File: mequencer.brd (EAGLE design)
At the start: 102.5 x 80 mm, 71 parts, among them IC1 NE555D, IC10 LF353D, IC11 NE555D, IC12 NE555D, IC2 4163D, IC3 74HC85D, IC4 4051D, IC5 4051D, IC6 74HCT04D, IC7 4051D, IC8 4051D, IC9 LF353D, U1 74LVC1G08SE-7

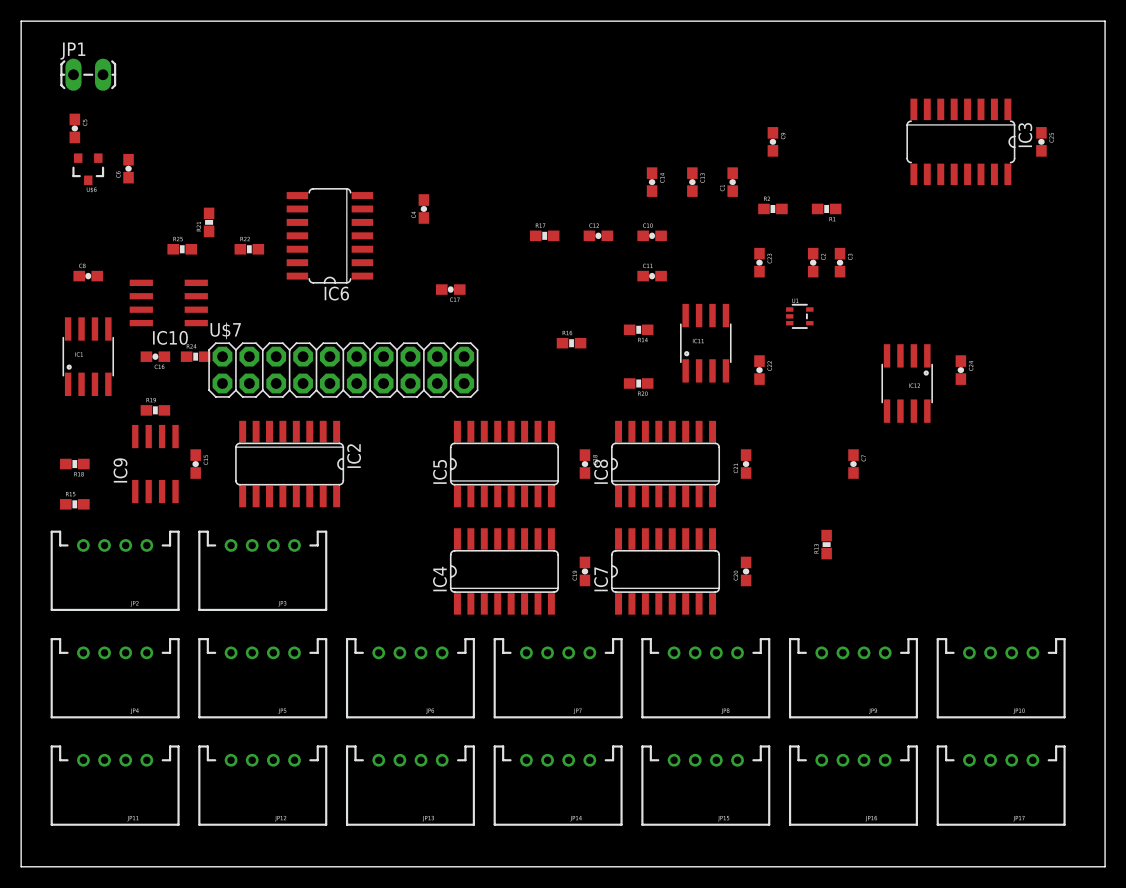
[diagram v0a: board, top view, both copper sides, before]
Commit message: through hole led on mini boards
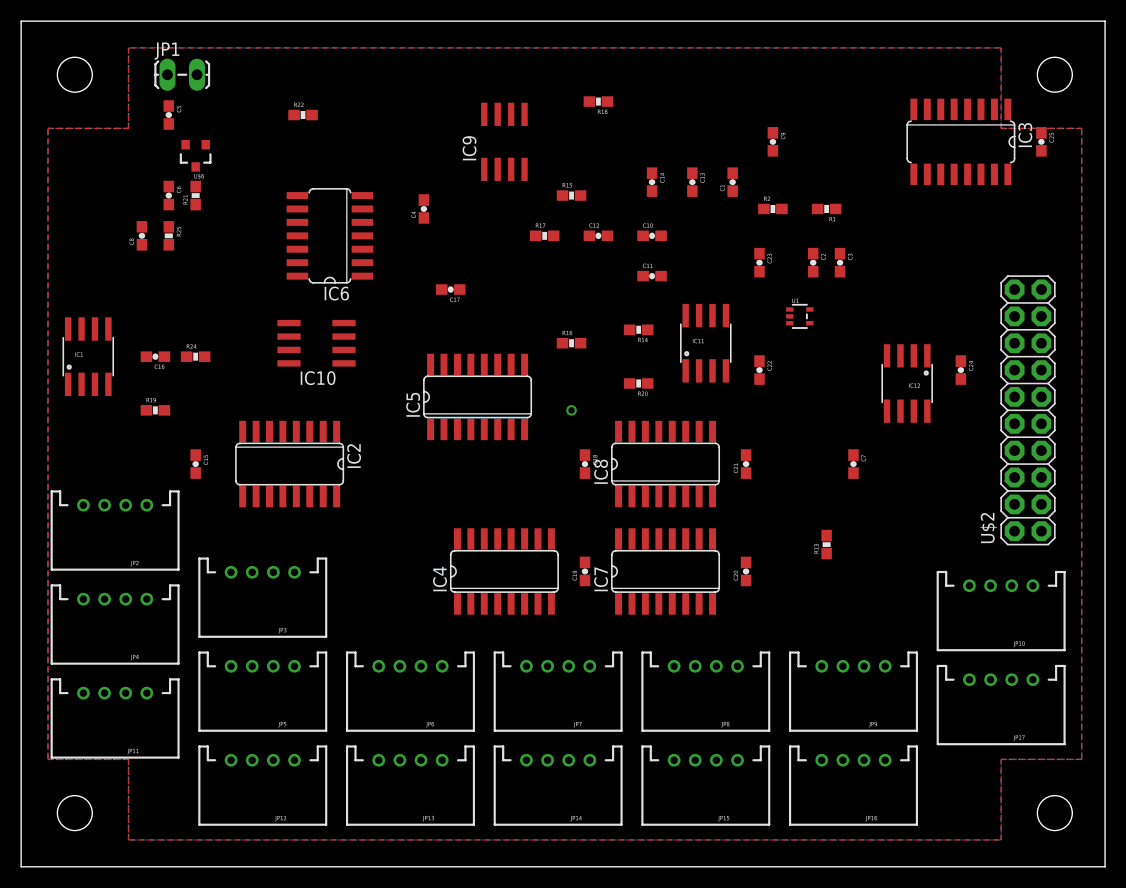
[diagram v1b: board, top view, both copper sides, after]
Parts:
- removed U$7: M10X2, SparkFun-Connectors:2X10
- added STANDOFF1, STANDOFF2, STANDOFF3, STANDOFF4: STAND-OFF, SparkFun-Electromechanical:STAND-OFF
- added U$2: M10X2, SparkFun-Connectors:2X10
- moved R18 60.2 mm to (50.8, 72.4)
- moved R15 55.3 mm to (48.3, 63.5)
- moved IC9 44.9 mm to (41.9, 68.6)
- moved IC10 14.5 mm to (24.1, 49.5)
- moved R22 13.7 mm to (22.9, 71.1)
- moved U$6 10.2 mm to (12.7, 67.3)
- moved C5 8.98 mm to (10.2, 71.1)
- moved JP1 8.89 mm to (10.2, 74.9)
- moved JP17 7.62 mm to (88.9, 12.7)
- moved IC5 6.84 mm to (39.4, 44.5)
- moved JP10 6.35 mm to (88.9, 21.6)
- moved JP11 6.35 mm to (5.08, 11.4)
- moved C8 6.35 mm to (7.62, 59.7), turned to 90 degrees
- moved JP4 5.08 mm to (5.08, 20.3)
- moved C6 4.58 mm to (10.2, 63.5), turned to 270 degrees
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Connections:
- removed net N$6: U$7.18
- net 5V: now also U$2.1; no longer U$7.1
- net CLOCK: now also U$2.5; no longer U$7.5
- net CLOCK_SPEED: now also U$2.7; no longer U$7.7
- net CV: now also U$2.17; no longer U$7.14
- net GND: now also U$2.20; no longer U$7.20
- net INT_CLOCK: now also U$2.3; no longer U$7.3
- net LOAD: now also U$2.11; no longer U$7.11
- net LOAD0: now also U$2.8; no longer U$7.6
- net LOAD1: now also U$2.6; no longer U$7.8
- net LOAD2: now also U$2.4; no longer U$7.10
- net LOAD3: now also U$2.2; no longer U$7.12
- net NOTE_LENGTH: now also U$2.9; no longer U$7.9
- net RESET0: now also U$2.16; no longer U$7.13
- net RESET1: now also U$2.14; no longer U$7.15
- net RESET2: now also U$2.12; no longer U$7.2
- net RESET3: now also U$2.10; no longer U$7.4
- net TRIG: now also U$2.19; no longer U$7.16
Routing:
- added copper zone on layer 16, net N$1
- added copper zone on layer 1, net N$5

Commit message: Moving shit around
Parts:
- moved C25 86.0 mm to (7.62, 55.9)
- moved R19 84.4 mm to (92.7, 53.3)
- moved R25 65.0 mm to (74.9, 54.6), turned to 0 degrees
- moved R22 64.8 mm to (81.3, 43.2), turned to 90 degrees
- moved R21 55.0 mm to (67.3, 57.1), turned to 270 degrees
- moved C2 53.9 mm to (19.1, 71.1), turned to 90 degrees
- moved R1 53.6 mm to (20.3, 74.9)
- moved R2 52.4 mm to (16.5, 74.9), turned to 90 degrees
- moved C1 51.2 mm to (12.7, 71.1), turned to 180 degrees
- moved IC10 50.3 mm to (73.7, 58.4)
- moved C11 50.2 mm to (7.62, 41.9), turned to 90 degrees
- moved C15 49.1 mm to (61.0, 29.2)
- moved IC9 48.1 mm to (88.9, 58.4), turned to 270 degrees
- moved C18 46.2 mm to (88.9, 62.2), turned to 0 degrees
- moved C4 44.6 mm to (78.7, 66.0), turned to 0 degrees
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
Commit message: Moving shit around more
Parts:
- removed C20, C21, C22, C23, C24, C25: .1uF, SparkFun-Capacitors:0603-CAP
- moved C15 59.6 mm to (7.62, 55.9)
- moved C16 41.3 mm to (73.7, 54.6), turned to 180 degrees
- moved C17 14.5 mm to (73.7, 40.6), turned to 180 degrees
- moved C18 14.0 mm to (88.9, 48.3)
- moved C4 10.5 mm to (81.3, 55.9)
- moved R25 8.98 mm to (73.7, 63.5)
- moved R19 8.98 mm to (91.4, 62.2), turned to 180 degrees
- moved R18 8.89 mm to (87.6, 62.2)
- moved C3 7.62 mm to (73.7, 48.3)
- moved R13 4.58 mm to (83.8, 40.6)
- moved R21 3.59 mm to (64.8, 59.7)
- moved R24 3.59 mm to (52.1, 41.9), turned to 180 degrees
- moved R22 2.54 mm to (81.3, 45.7), turned to 270 degrees
- moved R20 2.54 mm to (69.8, 63.5)
- moved C9 1.27 mm to (61.0, 69.8)
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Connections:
- net 5V: no longer C20.2, C21.2, C22.2, C23.2, C24.2, C25.2
- net N$7: no longer C20.1, C21.1, C22.1, C23.1, C24.1, C25.1

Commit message: stuff
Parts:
- moved IC5 43.5 mm to (50.2, 31.8), turned to 180 degrees
- moved C14 43.5 mm to (62.6, 41.5)
- moved R24 33.1 mm to (80.0, 59.7), turned to 0 degrees
- moved R14 30.0 mm to (66.7, 43.8), turned to 270 degrees
- moved C19 27.7 mm to (74.3, 24.8), turned to 180 degrees
- moved IC6 25.6 mm to (72.4, 32.4)
- moved IC8 25.3 mm to (35.6, 31.8), turned to 180 degrees
- moved C10 25.2 mm to (40.6, 25.4), turned to 180 degrees
- moved C9 24.8 mm to (36.2, 69.2), turned to 90 degrees
- moved IC7 22.4 mm to (50.2, 44.5), turned to 180 degrees
- moved IC4 21.7 mm to (35.6, 44.5), turned to 180 degrees
- moved U$2 16.0 mm to (58.4, 64.1), turned to 90 degrees
- moved C13 12.9 mm to (50.2, 59.1), turned to 90 degrees
- moved IC2 12.5 mm to (43.2, 59.1)
- moved IC3 10.2 mm to (43.2, 69.2), turned to 0 degrees
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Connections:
- removed net N$7: C10.1, C11.1, C12.1, C13.1, C14.1, C15.1, C16.1, C17.1, C18.1, C19.1, C7.1, C8.1, C9.1, IC10.8, IC2.16, IC3.16, IC4.16, IC5.16, IC6.14, IC7.16, IC8.16, IC9.8
- net 5V: now also IC10.8, IC2.16, IC3.16, IC4.16, IC5.16, IC6.14, IC7.16, IC8.16, IC9.8
- net GND: now also C10.1, C11.1, C12.1, C13.1, C14.1, C15.1, C16.1, C17.1, C18.1, C19.1, C7.1, C8.1, C9.1
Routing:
- net VCC: track 0.00 -> 110.3 mm
- net 5V: track 0.00 -> 102.1 mm
- net COUNT2: track 0.00 -> 60.1 mm
- net COUNT1: track 0.00 -> 59.6 mm, vias 0 -> 2
- net COUNT3: track 0.00 -> 25.0 mm, vias 0 -> 2
- net N$4: track 0.00 -> 15.5 mm
- net COUNT0: track 0.00 -> 13.2 mm
- net N$27: track 0.00 -> 6.96 mm
- net N$3: track 0.00 -> 5.42 mm
- net N$2: track 0.00 -> 2.35 mm
- added copper zone on layer 1, net GND
- added copper zone on layer 16, net GND
- removed copper zone on layer 16, net N$1
- removed copper zone on layer 1, net N$5

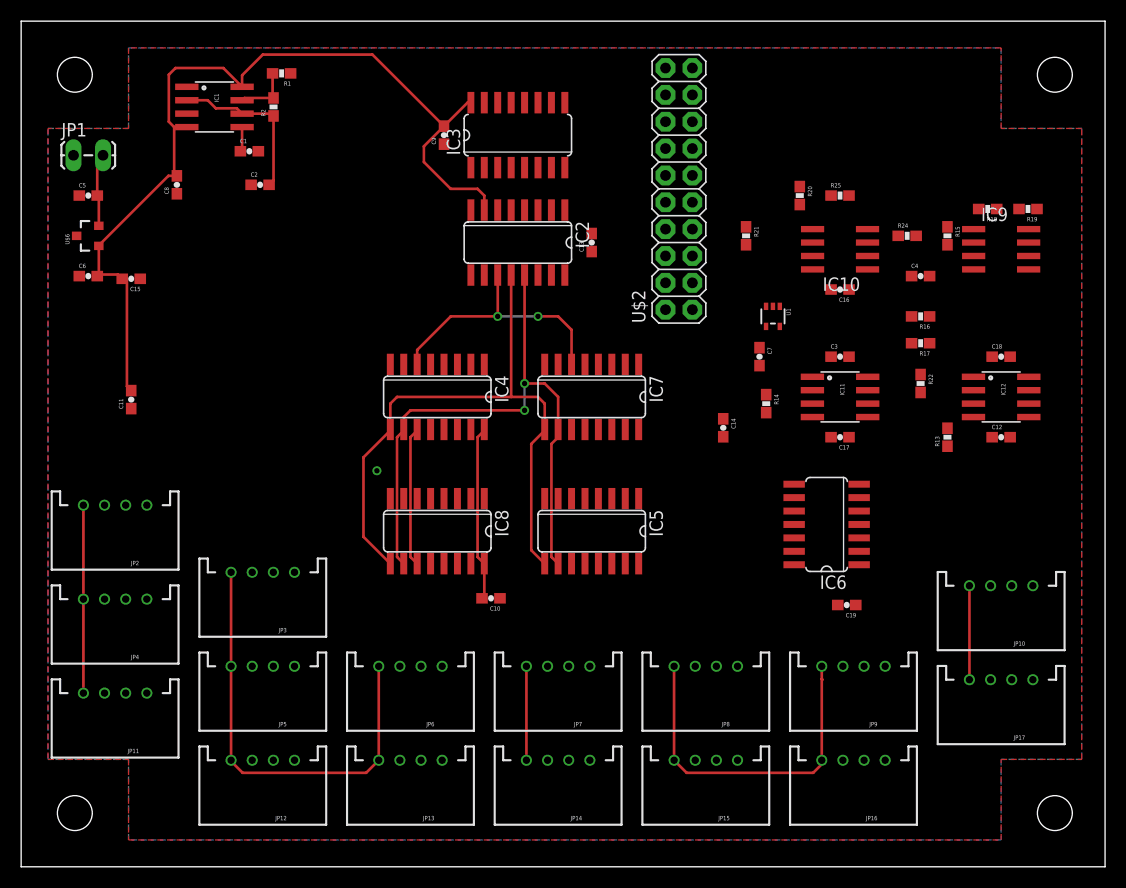
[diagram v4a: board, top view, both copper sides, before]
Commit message: Muxxes all wired up
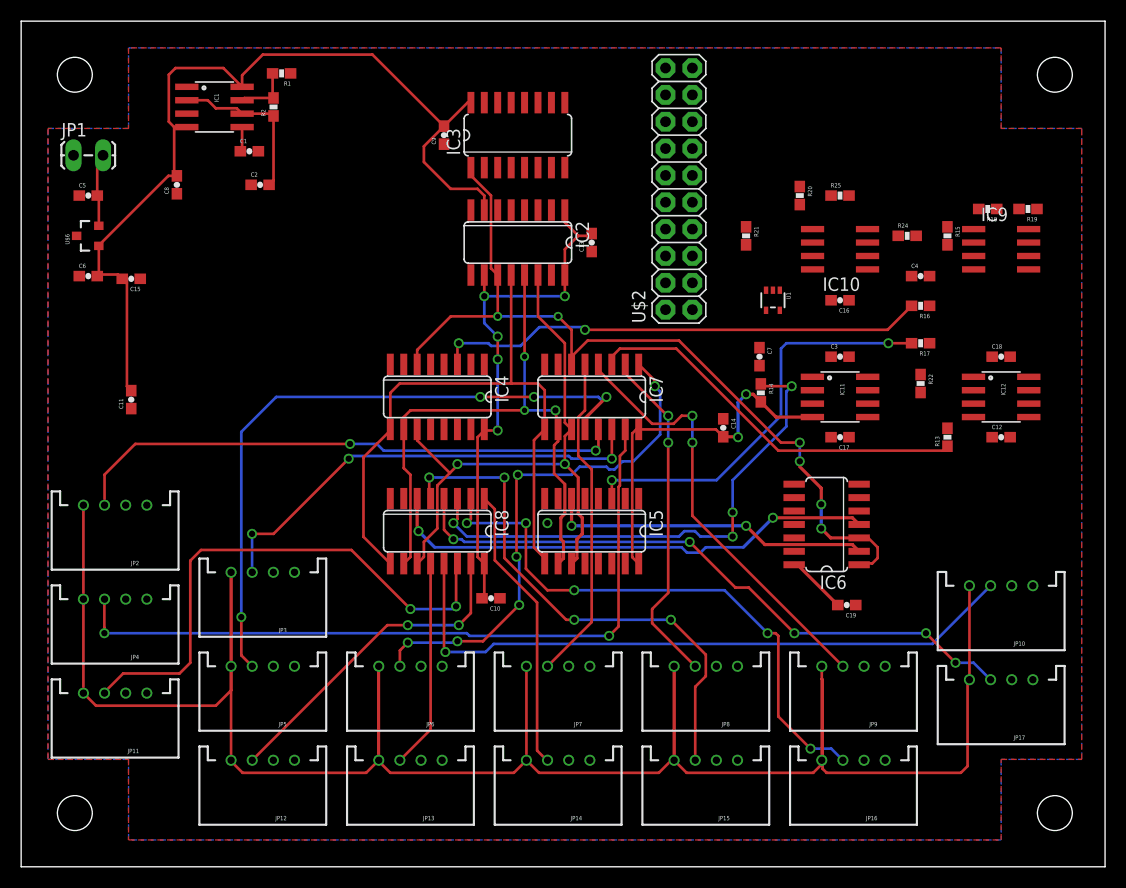
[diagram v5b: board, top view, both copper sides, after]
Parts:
- moved U1 1.52 mm to (67.3, 53.6)
- moved R14 1.14 mm to (66.2, 44.8)
- moved C16 1.02 mm to (73.7, 53.6)
- moved R16 1.00 mm to (81.3, 53.1)
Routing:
- net VCC: track 110.3 -> 215.0 mm
- net 5V: track 102.1 -> 177.1 mm, vias 0 -> 7
- net LED2: track 0.00 -> 71.2 mm, vias 0 -> 2
- net LED3: track 0.00 -> 62.7 mm, vias 0 -> 4
- net LED8: track 0.00 -> 62.6 mm, vias 0 -> 1
- net LED15: track 0.00 -> 60.5 mm, vias 0 -> 5
- net COUNT3: track 25.0 -> 81.2 mm, vias 2 -> 6
- net LED14: track 0.00 -> 54.3 mm, vias 0 -> 5
- net LED0: track 0.00 -> 52.9 mm, vias 0 -> 2
- net LED9: track 0.00 -> 51.1 mm, vias 0 -> 2
- net LED13: track 0.00 -> 50.0 mm, vias 0 -> 4
- net LED4: track 0.00 -> 49.8 mm, vias 0 -> 6
- net N$19: track 0.00 -> 49.4 mm, vias 0 -> 4
- net N$9: track 0.00 -> 47.3 mm, vias 0 -> 2
- net LOW_OUT: track 0.00 -> 46.8 mm, vias 0 -> 2
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
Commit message: main board all wired up
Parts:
- moved IC3 14.5 mm to (28.7, 69.2)
- moved C13 14.0 mm to (36.2, 57.9)
- moved IC2 14.0 mm to (29.2, 58.0)
- moved C9 14.0 mm to (22.2, 69.2)
- moved R21 3.94 mm to (68.7, 59.8)
- moved R24 1.17 mm to (79.8, 60.8), turned to 90 degrees
- moved R15 1.17 mm to (83.1, 60.6)
- moved C3 0.28 mm to (73.5, 48.5)
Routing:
- net 5V: track 177.1 -> 308.4 mm, vias 7 -> 17
- net CLOCK: track 0.00 -> 81.7 mm, vias 0 -> 4
- net CLOCK_SPEED: track 0.00 -> 62.7 mm
- net NOTE_LENGTH: track 0.00 -> 61.8 mm, vias 0 -> 2
- net INT_CLOCK: track 0.00 -> 60.0 mm
- net LOAD: track 0.00 -> 54.4 mm, vias 0 -> 2
- net CV: track 0.00 -> 51.6 mm, vias 0 -> 4
- net RESET3: track 0.00 -> 38.9 mm, vias 0 -> 2
- net LOAD3: track 0.00 -> 34.4 mm, vias 0 -> 2
- net RESET2: track 0.00 -> 33.2 mm
- net LOAD1: track 0.00 -> 32.5 mm, vias 0 -> 2
- net LOAD2: track 0.00 -> 32.4 mm, vias 0 -> 2
- net COUNT0: track 56.6 -> 88.8 mm, vias 2 -> 6
- net RESET1: track 0.00 -> 31.5 mm
- net LOAD0: track 0.00 -> 28.8 mm
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
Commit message: changed some 1ks to 100ks to draw less current
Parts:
- R20, R21: value 1k -> 100k
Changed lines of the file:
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@@
 <setting verticaltext="up"/>
 </settings>
-<grid distance="5" unitdist="mil" unit="mil" style="lines" multiple="1" display="yes" altdistance="0.005" altunitdist="inch" altunit="inch"/>
+<grid distance="0.05" unitdist="inch" unit="inch" style="lines" multiple="1" display="yes" altdistance="0.005" altunitdist="inch" altunit="inch"/>
 <layers>
 <layer number="1" name="Top" color="4" fill="1" visible="yes" active="yes"/>
@@
 <layer number="19" name="Unrouted" color="6" fill="1" visible="yes" active="yes"/>
 <layer number="20" name="Dimension" color="15" fill="1" visible="yes" active="yes"/>
-<layer number="21" name="tPlace" color="7" fill="1" visible="yes" active="yes"/>
-<layer number="22" name="bPlace" color="7" fill="1" visible="yes" active="yes"/>
+<layer number="21" name="tPlace" color="16" fill="1" visible="yes" active="yes"/>
+<layer number="22" name="bPlace" color="14" fill="1" visible="yes" active="yes"/>
 <layer number="23" name="tOrigins" color="15" fill="1" visible="yes" active="yes"/>
 <layer number="24" name="bOrigins" color="15" fill="1" visible="yes" active="yes"/>
@@
 <layer number="49" name="Reference" color="7" fill="1" visible="no" active="yes"/>
 <layer number="50" name="dxf" color="7" fill="1" visible="no" active="no"/>
-<layer number="51" name="tDocu" color="7" fill="1" visible="yes" active="yes"/>
+<layer number="51" name="tDocu" color="6" fill="1" visible="yes" active="yes"/>
 <layer number="52" name="bDocu" color="7" fill="1" visible="no" active="yes"/>
 <layer number="53" name="tGND_GNDA" color="7" fill="9" visible="no" active="no"/>
@@
 <element name="R19" library="SparkFun-Resistors" package="0603-RES" value="1k" x="91.44" y="62.23" rot="R180"/>
 <element name="IC10" library="linear" package="SO08" value="LF353D" x="73.66" y="58.42" rot="R90"/>
-<element name="R20" library="SparkFun-Resistors" package="0603-RES" value="1k" x="69.85" y="63.5" rot="R270"/>
-<element name="R21" library="SparkFun-Resistors" package="0603-RES" value="1k" x="68.707" y="59.817" rot="R270"/>
+<element name="R20" library="SparkFun-Resistors" package="0603-RES" value="100k" x="69.85" y="63.5" rot="R270"/>
+<element name="R21" library="SparkFun-Resistors" package="0603-RES" value="100k" x="68.707" y="59.817" rot="R270"/>
 <element name="IC11" library="SparkFun-AnalogIC" package="SO08" value="NE555D" x="73.66" y="44.45" rot="R270"/>
 <element name="IC12" library="SparkFun-AnalogIC" package="SO08" value="NE555D" x="88.9" y="44.45" rot="R270"/>

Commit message: bumped the resistance values in the CV summer so that the resistance in note pot won't affect the note's CV when it is in rest mode
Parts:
- R15, R16, R17: value 100k -> 1M
- R18, R19: value 1k -> 10k
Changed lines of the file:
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@@
 <element name="R14" library="SparkFun-Resistors" package="0603-RES" value="" x="66.167" y="44.831" rot="R270"/>
 <element name="IC9" library="linear" package="SO08" value="LF353D" x="88.9" y="58.42" rot="R270"/>
-<element name="R15" library="SparkFun-Resistors" package="0603-RES" value="100k" x="83.058" y="60.579" rot="R270"/>
-<element name="R16" library="SparkFun-Resistors" package="0603-RES" value="100k" x="81.28" y="53.07" rot="R180"/>
-<element name="R17" library="SparkFun-Resistors" package="0603-RES" value="100k" x="81.28" y="49.53" rot="R180"/>
-<element name="R18" library="SparkFun-Resistors" package="0603-RES" value="1k" x="87.63" y="62.23" rot="R180"/>
-<element name="R19" library="SparkFun-Resistors" package="0603-RES" value="1k" x="91.44" y="62.23" rot="R180"/>
+<element name="R15" library="SparkFun-Resistors" package="0603-RES" value="1M" x="83.058" y="60.579" rot="R270"/>
+<element name="R16" library="SparkFun-Resistors" package="0603-RES" value="1M" x="81.28" y="53.07" rot="R180"/>
+<element name="R17" library="SparkFun-Resistors" package="0603-RES" value="1M" x="81.28" y="49.53" rot="R180"/>
+<element name="R18" library="SparkFun-Resistors" package="0603-RES" value="10k" x="87.63" y="62.23" rot="R180"/>
+<element name="R19" library="SparkFun-Resistors" package="0603-RES" value="10k" x="91.44" y="62.23" rot="R180"/>
 <element name="IC10" library="linear" package="SO08" value="LF353D" x="73.66" y="58.42" rot="R90"/>
 <element name="R20" library="SparkFun-Resistors" package="0603-RES" value="100k" x="69.85" y="63.5" rot="R270"/>
